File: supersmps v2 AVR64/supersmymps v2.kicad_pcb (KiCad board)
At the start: 2 copper layers, 200 x 140 mm, 134 parts, among them J2 programmer, J3 Front_Panel, J4 Conn_01x03_Socket, J5 Wire (it's copper), Q1 IRFP360, Q2 IRFP360, Q3 IRFP360, Q4 IRFP360, Q5 IRFP360, Q6 IRFZ44N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

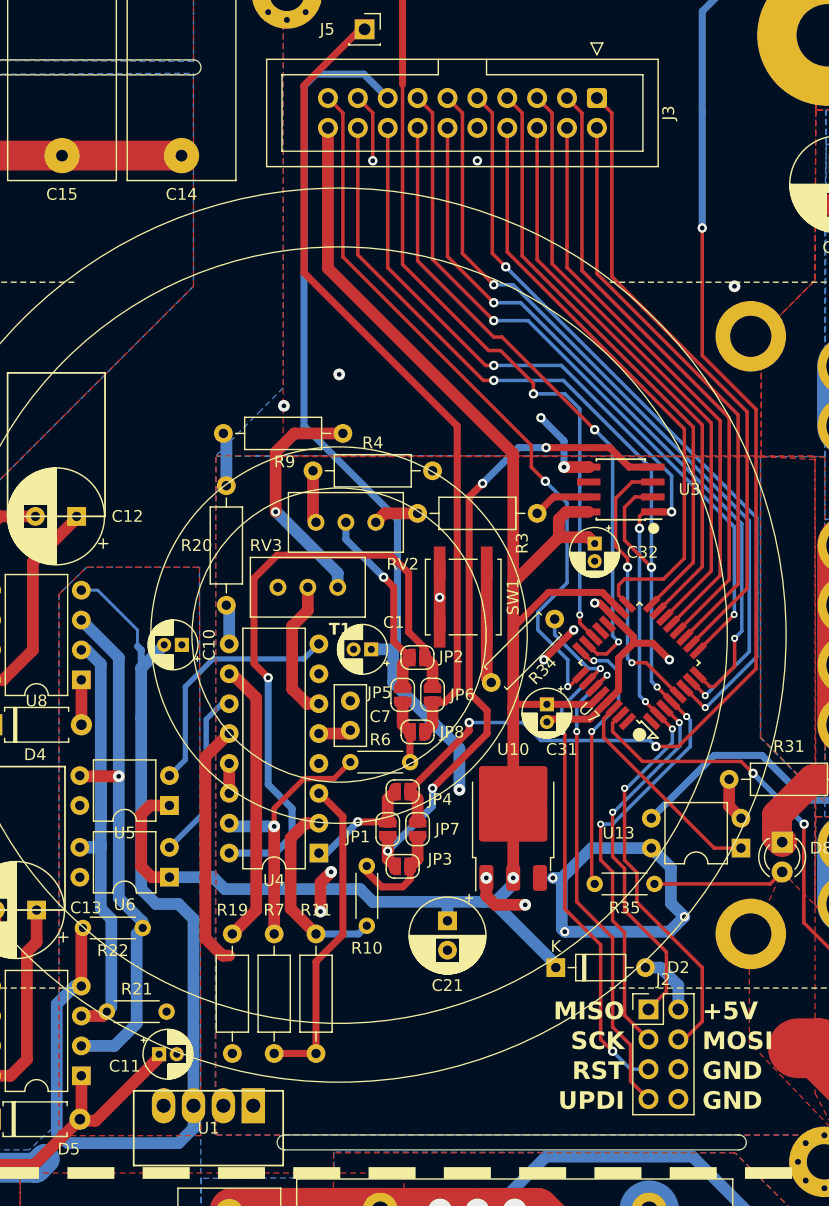
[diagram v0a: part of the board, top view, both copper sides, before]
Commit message: One of the last versions before prototype is done.
I have finally gotten rid of the solder jumpers because i'm now sure how the tl494 circuit works
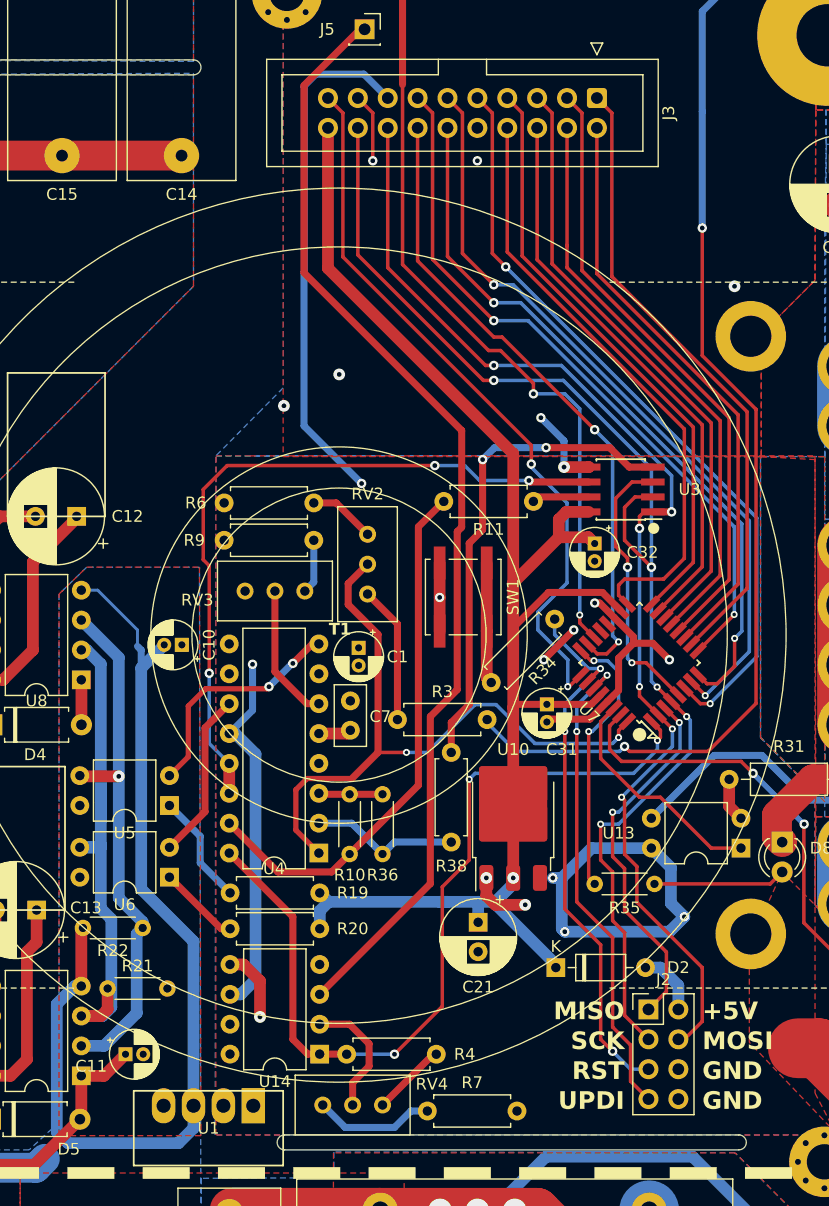
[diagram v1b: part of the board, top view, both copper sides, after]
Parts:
- removed JP1, JP2, JP7, JP8: B, Jumper:SolderJumper-2_P1.3mm_Open_RoundedPad1.0x1.5mm
- removed JP3, JP4, JP5, JP6: A, Jumper:SolderJumper-2_P1.3mm_Open_RoundedPad1.0x1.5mm
- added R36: 10k, Resistor_THT:R_Axial_DIN0204_L3.6mm_D1.6mm_P5.08mm_Horizontal, F.Cu at (123.7, 91.9)
- added R38: 22, Resistor_THT:R_Axial_DIN0207_L6.3mm_D2.5mm_P7.62mm_Horizontal, F.Cu at (129.5, 88.4)
- added RV4: 10k, Potentiometer_THT:Potentiometer_Bourns_3296W_Vertical, F.Cu at (118.6, 118.4)
- added U14: NE5532, Package_DIP:DIP-8_W7.62mm, F.Cu at (118.4, 114.0)
- C7: value 10n -> 1n
- R10, RV3: value 1k -> 10k
- R11: value 100k -> 22; footprint Resistor_THT:R_Axial_DIN0207_L6.3mm_D2.5mm_P10.16mm_Horizontal -> Resistor_THT:R_Axial_DIN0207_L6.3mm_D2.5mm_P7.62mm_Horizontal
- R19, R20: footprint Resistor_THT:R_Axial_DIN0207_L6.3mm_D2.5mm_P10.16mm_Horizontal -> Resistor_THT:R_Axial_DIN0207_L6.3mm_D2.5mm_P7.62mm_Horizontal
- R3: value 100k -> 330k; footprint Resistor_THT:R_Axial_DIN0207_L6.3mm_D2.5mm_P10.16mm_Horizontal -> Resistor_THT:R_Axial_DIN0207_L6.3mm_D2.5mm_P7.62mm_Horizontal
- R4: value 500 -> 560k; footprint Resistor_THT:R_Axial_DIN0207_L6.3mm_D2.5mm_P10.16mm_Horizontal -> Resistor_THT:R_Axial_DIN0207_L6.3mm_D2.5mm_P7.62mm_Horizontal
- R6: value 1k -> 36k; footprint Resistor_THT:R_Axial_DIN0204_L3.6mm_D1.6mm_P5.08mm_Horizontal -> Resistor_THT:R_Axial_DIN0207_L6.3mm_D2.5mm_P7.62mm_Horizontal
- R7: value 100k -> 6.8k; footprint Resistor_THT:R_Axial_DIN0207_L6.3mm_D2.5mm_P10.16mm_Horizontal -> Resistor_THT:R_Axial_DIN0207_L6.3mm_D2.5mm_P7.62mm_Horizontal
- R9: value 500 -> 5.1k; footprint Resistor_THT:R_Axial_DIN0207_L6.3mm_D2.5mm_P10.16mm_Horizontal -> Resistor_THT:R_Axial_DIN0207_L6.3mm_D2.5mm_P7.62mm_Horizontal
- moved R4 50.7 mm to (128.3, 114.0), turned to 180 degrees
- moved R11 41.1 mm to (136.5, 67.1), turned to 180 degrees
- moved R20 28.6 mm to (118.4, 103.4), turned to 180 degrees
- moved R6 27.1 mm to (110.2, 67.2), turned to 0 degrees
- moved R7 21.2 mm to (135.1, 118.9), turned to 180 degrees
- moved R3 17.6 mm to (125.0, 85.6)
- moved R9 9.41 mm to (117.9, 70.4)
- moved R19 8.21 mm to (118.4, 100.3), turned to 180 degrees
- moved RV2 6.14 mm to (122.4, 74.9), turned to -90 degrees
- moved C11 2.86 mm to (101.9, 114.0)
- moved RV3 2.81 mm to (112.0, 74.7)
- moved C21 2.61 mm to (131.8, 102.8)
- moved R21 1.97 mm to (100.3, 108.5)
- moved R10 1.78 mm to (120.9, 97.0), turned to 90 degrees
- moved C1 1.08 mm to (121.7, 79.5), turned to -90 degrees
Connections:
- R10 pad 1: Net-(JP3-B) -> Net-(U4-2IN-)
- R10 pad 2: ADC0 -> Net-(U4-FB)
- R11 pad 1: ADC0 -> DAC_CUR
- R11 pad 2: Net-(U4-FB) -> Net-(U4-2IN-)
- R19 pad 1: Net-(U4-E2) -> +5V
- R19 pad 2: GND1 -> Net-(R19-Pad2)
- R20 pad 1: Net-(U4-E1) -> +5V
- R20 pad 2: GND1 -> Net-(R20-Pad2)
- R3 pad 2: OUT_B -> VDC
- R4 pad 2: GND1 -> ADC_CUR
- R6 pad 1: Net-(JP5-B) -> GND1
- R6 pad 2: ADC1 -> Net-(R6-Pad2)
- R7 pad 1: Net-(U4-FB) -> GND1
- R7 pad 2: ADC1 -> Net-(R7-Pad2)
- RV2 pad 2: Net-(JP2-A) -> ADC_VOL
- RV2 pad 3: Net-(R4-Pad1) -> Net-(R6-Pad2)
- U3 pad 4: OUT_A -> DAC_VOL
- U3 pad 6: Net-(U3-REF) -> DAC_REF
- U3 pad 7: OUT_B -> DAC_CUR
- U4 pad 1: Net-(JP1-B) -> ADC_VOL
- U4 pad 10: Net-(U4-E2) -> GND1
- U4 pad 13: Net-(U4-OUTCTRL) -> DAC_REF
- U4 pad 14: Net-(U4-OUTCTRL) -> DAC_REF
- U4 pad 15: ADC1 -> Net-(U4-2IN-)
- U4 pad 16: 2IN+ -> ADC_CUR
- U4 pad 2: ADC0 -> Net-(U4-1IN-)
- U4 pad 9: Net-(U4-E1) -> GND1
- U5 pad 1: +5V -> Net-(R19-Pad2)
- U6 pad 1: +5V -> Net-(R20-Pad2)
- U7 pad 1: ADC1 -> ADC_CUR
- U7 pad 32: ADC0 -> ADC_VOL
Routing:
- net ADC_CUR: track 0.00 -> 73.1 mm, vias 0 -> 3
- net DAC_REF: track 0.00 -> 60.9 mm, vias 0 -> 3
- net ADC_VOL: track 0.00 -> 57.6 mm, vias 0 -> 2
- net OUT_A: track 55.0 -> 0.00 mm, vias 4 -> 0
- net 2IN+: track 54.3 -> 0.00 mm, vias 1 -> 0
- net Net-(U4-2IN-): track 0.00 -> 46.3 mm
- net DAC_VOL: track 0.00 -> 41.6 mm, vias 0 -> 2
- net IBUS: track 69.2 -> 94.9 mm
- net Net-(U4-E2): track 24.1 -> 0.00 mm
- net ADC1: track 22.7 -> 0.00 mm, vias 1 -> 0
- net Net-(U4-FB): track 27.5 -> 5.50 mm
- net +12V: track 308.6 -> 287.6 mm, vias 4 -> 5
- net +5V: track 153.2 -> 133.3 mm
- net ADC0: track 16.6 -> 0.00 mm
- net Net-(JP2-A): track 16.5 -> 0.00 mm, vias 1 -> 0
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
